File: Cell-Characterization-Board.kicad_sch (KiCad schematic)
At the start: 1 part, among them U1 ESP32-S3-WROOM-1

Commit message: 🤪
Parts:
- added D1, D2, D3, D4: SBR10E45P5-7, SBR10E45P57, symbol SBR10E45P5-7:SBR10E45P5-7
- added IC1, IC2, IC3, IC4: CPC1006N, SOP254P610X216-4N, symbol CPC1006N:CPC1006N
- added K1, K2, K3, K4: V23105A5001A201, V23105A5001A201, symbol V23105A5001A201:V23105A5001A201
- added RT1, RT2, RT3, RT4: NCP18XH103F03RB, THRMC1608X95N, symbol NCP18XH103F03RB:NCP18XH103F03RB
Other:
- added sheet ADC (ADC.kicad_sch)
- added sheet Cell1 (Cell.kicad_sch)
- added sheet Cell2 (Cell.kicad_sch)
- added sheet Cell3 (Cell.kicad_sch)
- added sheet Cell4 (Cell.kicad_sch)
- added sheet Power (Power.kicad_sch)
- moved on the sheet: U1

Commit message: Updated main schematic
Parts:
- removed D1, D2, D3, D4: SBR10E45P5-7, SBR10E45P57, symbol SBR10E45P5-7:SBR10E45P5-7
- removed IC1, IC2, IC3, IC4: CPC1006N, SOP254P610X216-4N, symbol CPC1006N:CPC1006N
- removed K1, K2, K3, K4: V23105A5001A201, V23105A5001A201, symbol V23105A5001A201:V23105A5001A201
- removed RT1, RT2, RT3, RT4: NCP18XH103F03RB, THRMC1608X95N, symbol NCP18XH103F03RB:NCP18XH103F03RB
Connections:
- net GND: now also U1.1 (GND), U1.40 (GND), U1.41 (GND)
- net GPIO17: now reaches U1.10 (IO17)
- net GPIO18: now reaches U1.11 (IO18)
- net PWM2: now reaches U1.12 (IO8)
- net ADC1_2: now reaches U1.15 (IO3)
- net PWM1: now reaches U1.17 (IO9)
- net PWM0: now reaches U1.18 (IO10)
- net ADC2_0: now reaches U1.19 (IO11)
- net +3V3: now reaches U1.2 (3V3)
- net ADC2_1: now reaches U1.20 (IO12)
- net ADC2_2: now reaches U1.21 (IO13)
- net ADC2_3: now reaches U1.22 (IO14)
- net GPIO0: now reaches U1.27 (IO0)
- net ADC1_1: now reaches U1.31 (IO38)
- net ADC1_0: now reaches U1.32 (IO39)
- net GPIO2: now reaches U1.38 (IO2)
- net GPIO1: now reaches U1.39 (IO1)
- net ADC1_3: now reaches U1.4 (IO4)
- net GPIO5: now reaches U1.5 (IO5)
- net GPIO6: now reaches U1.6 (IO6)
- net PWM3: now reaches U1.7 (IO7)
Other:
- note added: "INT"
- moved on the sheet: U1

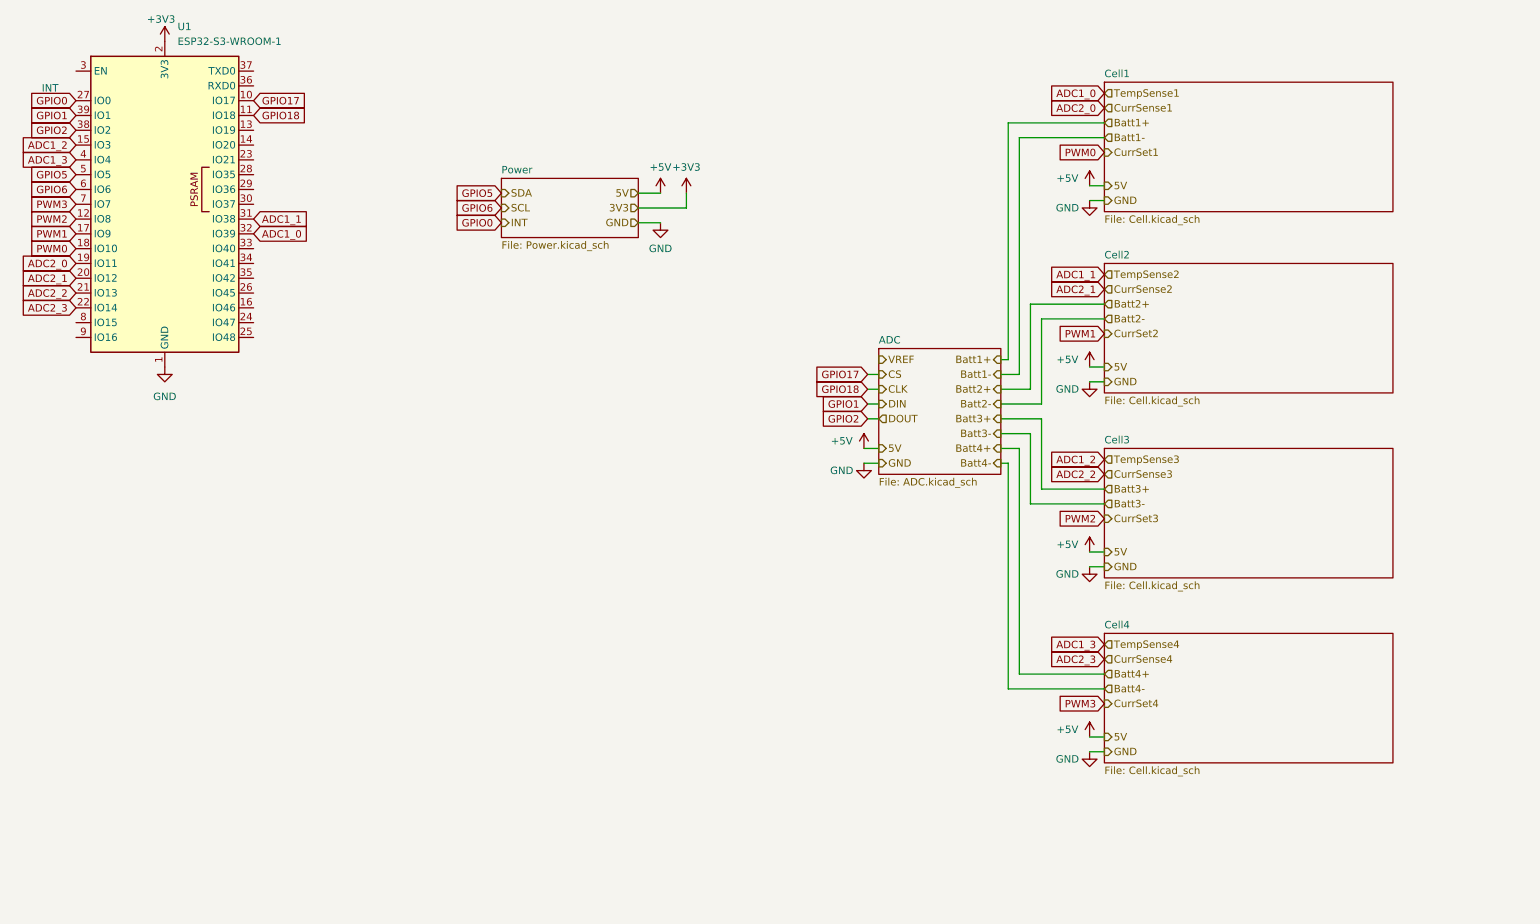
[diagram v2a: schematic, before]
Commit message: Added a few more components to the sch
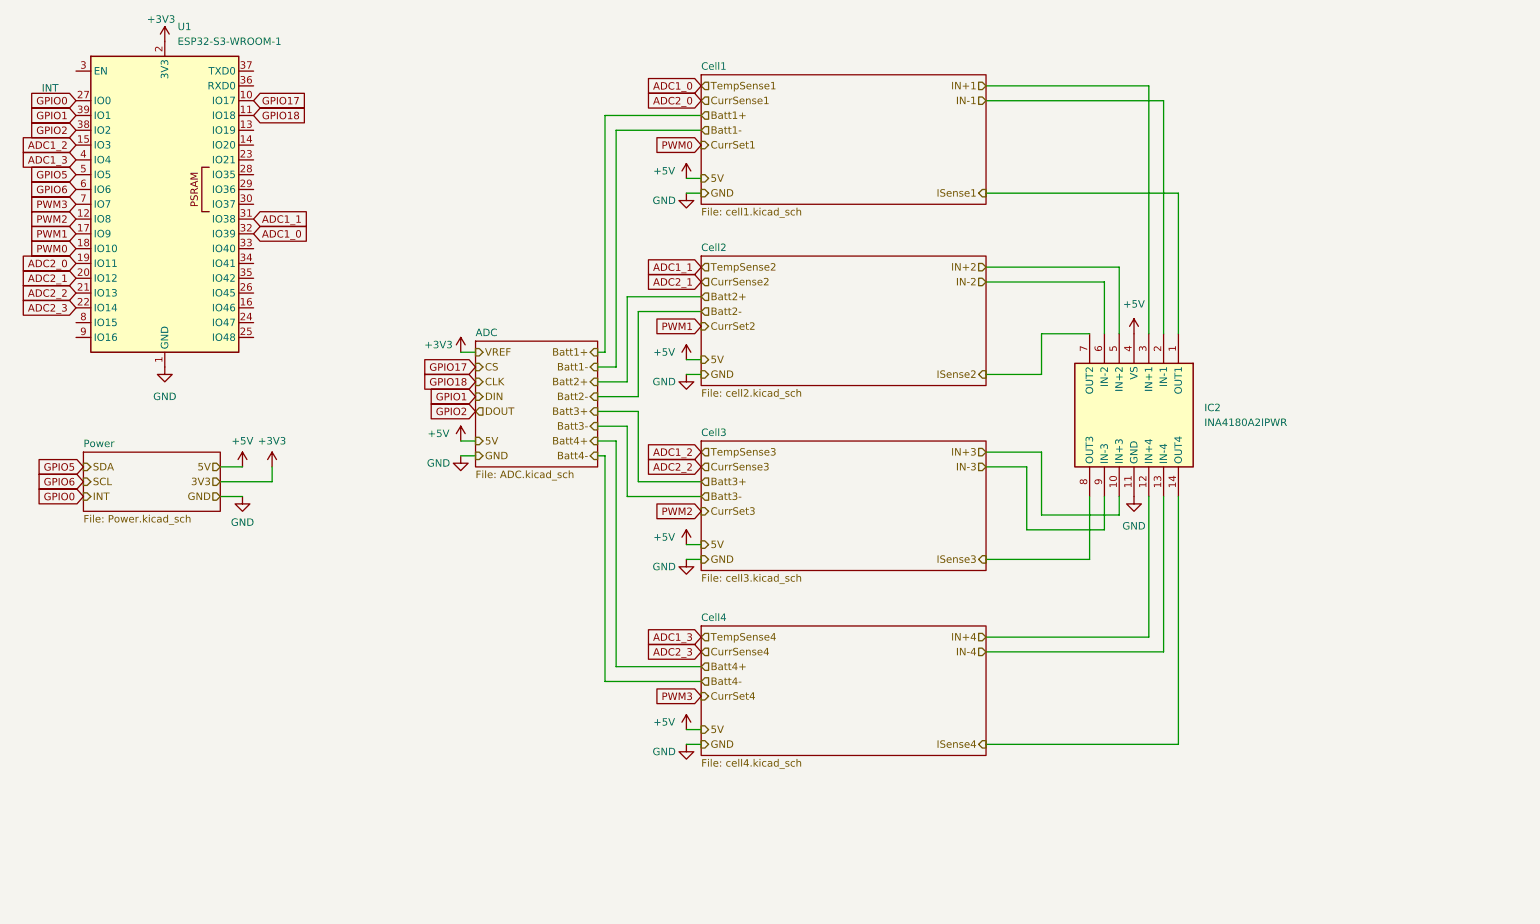
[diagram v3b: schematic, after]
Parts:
- added IC2: INA4180A2IPWR, SOP65P640X120-14N, symbol INA4180A2IPWR:INA4180A2IPWR
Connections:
- net +5V: now also IC2.4 (VS)
- net GND: now also IC2.11 (GND)
- new net IN+1: IC2.3 (IN+1)
- new net IN+2: IC2.5 (IN+2)
- new net IN+3: IC2.10 (IN+3)
- new net IN+4: IC2.12 (IN+4)
- new net IN-1: IC2.2 (IN-1)
- new net IN-2: IC2.6 (IN-2)
- new net IN-3: IC2.9 (IN-3)
- new net IN-4: IC2.13 (IN-4)
- new net ISense1: IC2.1 (OUT1)
- new net ISense2: IC2.7 (OUT2)
- new net ISense3: IC2.8 (OUT3)
- new net ISense4: IC2.14 (OUT4)
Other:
- sheet Cell1: file Cell.kicad_sch -> cell1.kicad_sch
- sheet Cell2: file Cell.kicad_sch -> cell2.kicad_sch
- sheet Cell3: file Cell.kicad_sch -> cell3.kicad_sch
- sheet Cell4: file Cell.kicad_sch -> cell4.kicad_sch

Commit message: updated power stuff
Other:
- note added: "ESP32"
- note added: "External ADC"
- note added: "Individual Cell Modules"
- note added: "USB-C PD Power Delivery"
- moved on the sheet: IC2, U1

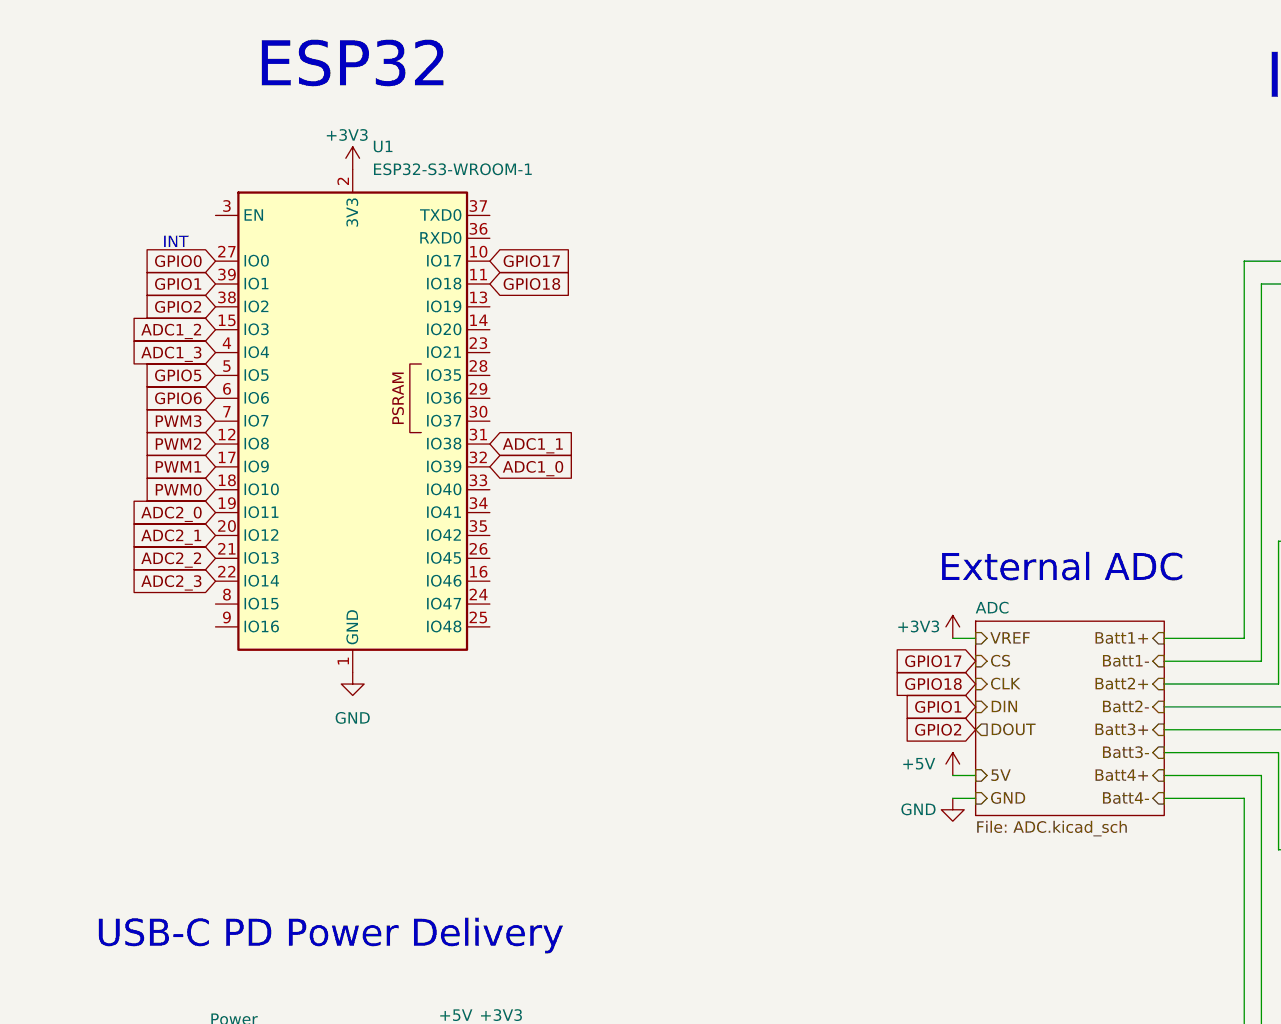
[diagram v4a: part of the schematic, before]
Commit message: began adding USB-UART bridge
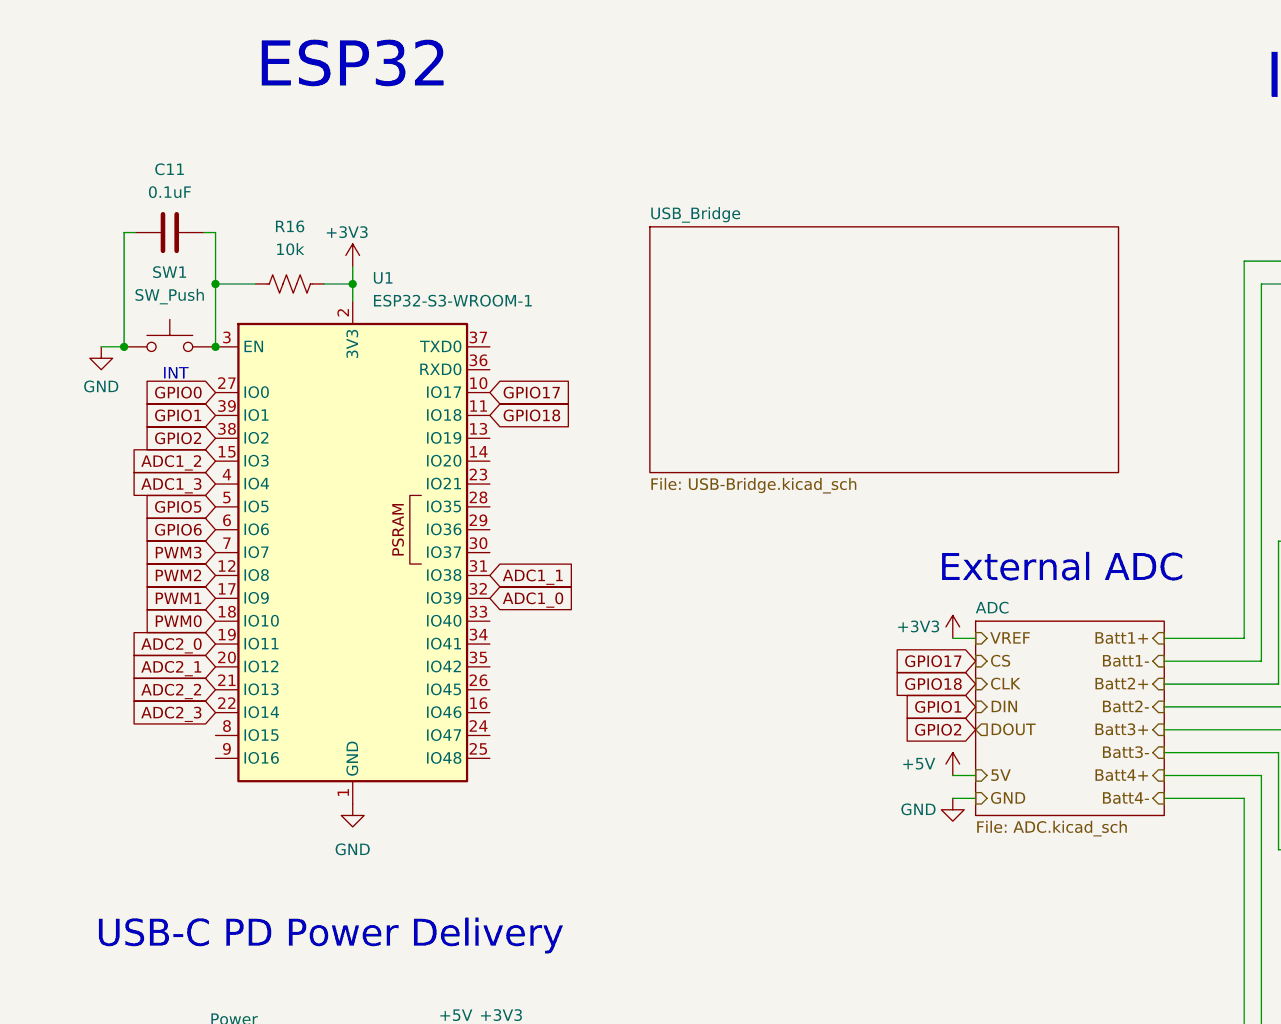
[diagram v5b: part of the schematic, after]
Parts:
- added C11: 0.1uF, symbol Device:C
- added R16: 10k, symbol Device:R_US
- added SW1: SW_Push, symbol Switch:SW_Push
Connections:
- net +3V3: now also R16.2
- net GND: now also C11.1, SW1.1
- net at U1.3 (EN): now also C11.2, R16.1, SW1.2
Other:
- added sheet USB_Bridge (USB-Bridge.kicad_sch)
- moved on the sheet: U1

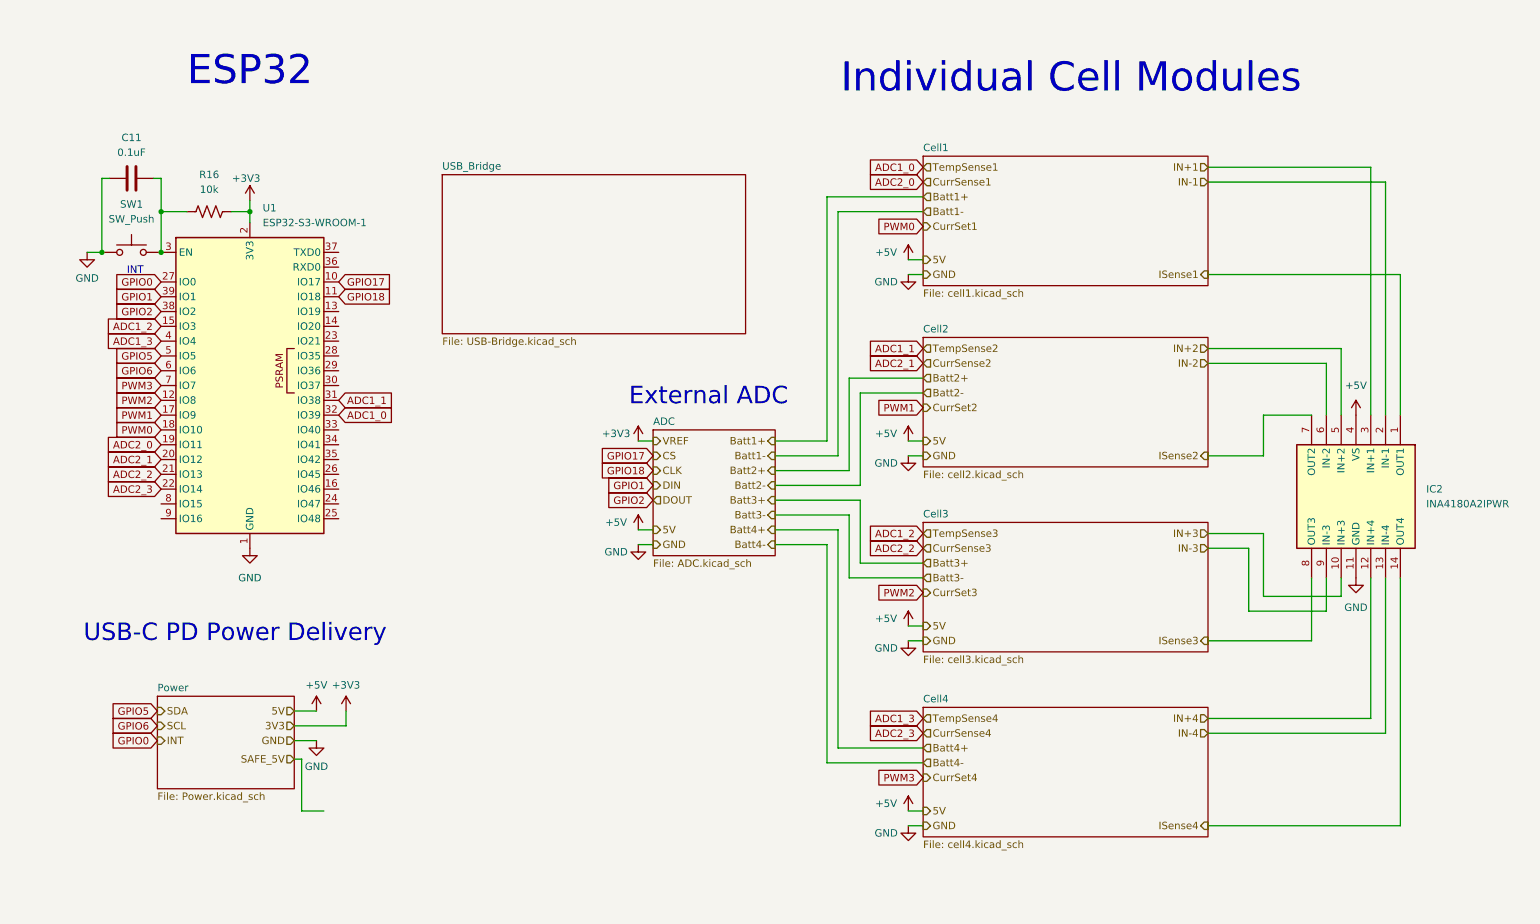
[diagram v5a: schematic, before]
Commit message: usb uart fixes and ldo
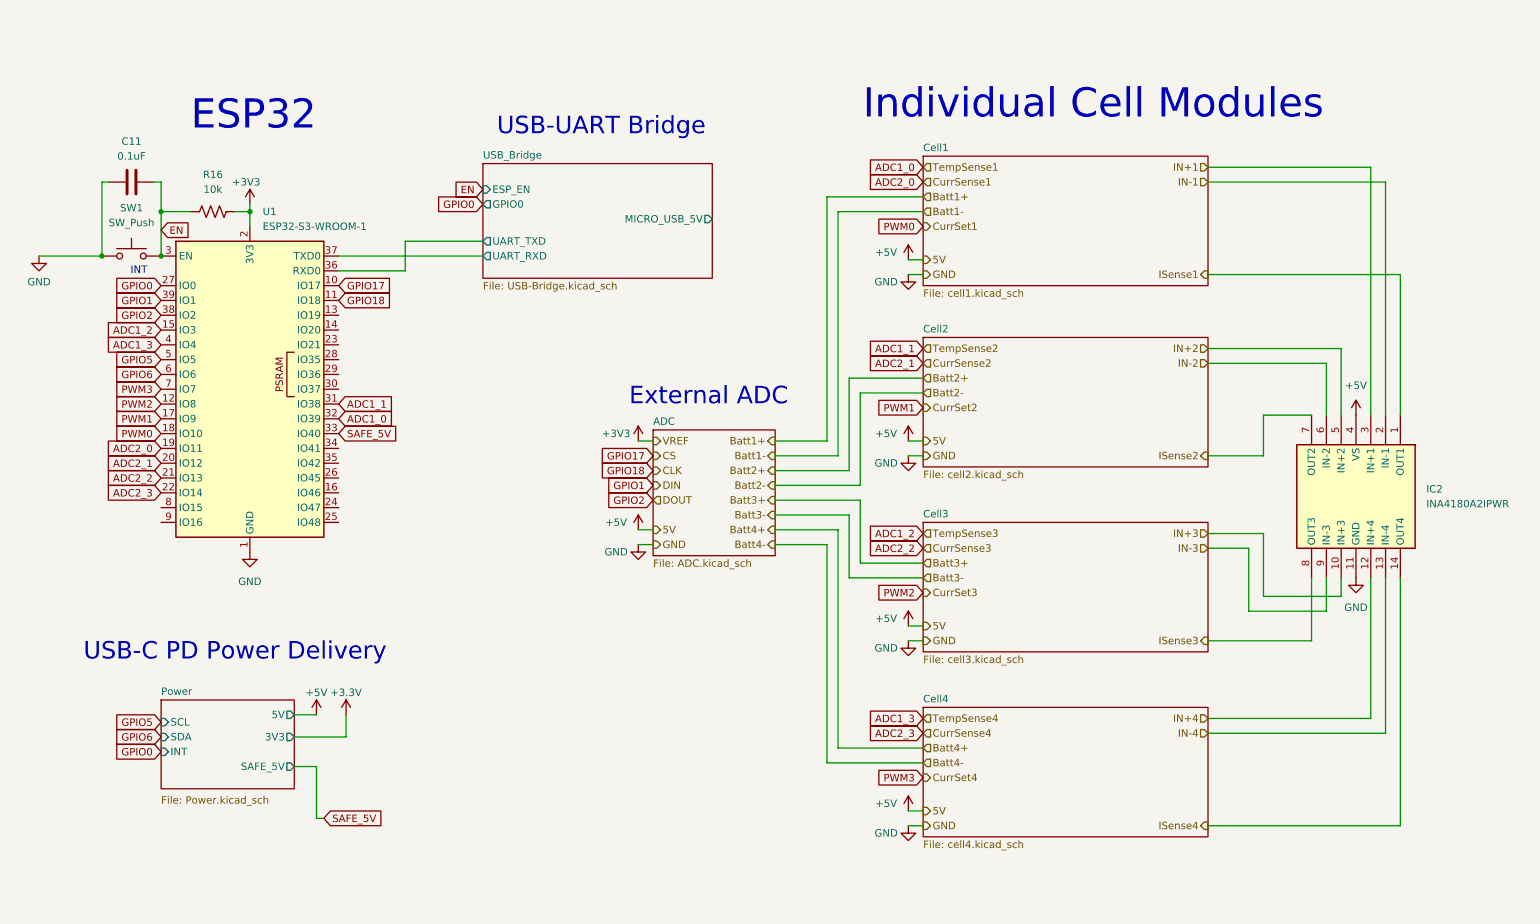
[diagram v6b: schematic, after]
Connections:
- net SAFE_5V: now also U1.33 (IO40)
- net EN: now reaches C11.2, R16.1, SW1.2, U1.3 (EN)
- net USB_Bridge/UART_TXD: now reaches U1.36 (RXD0)
- net USB_Bridge/UART_RXD: now reaches U1.37 (TXD0)
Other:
- sheet Power ports: added 3V3, 5V, INT, SAFE_5V, SCL, SDA; removed none
- sheet USB_Bridge ports: added ESP_EN, GPIO0, MICRO_USB_5V, UART_RXD, UART_TXD; removed none
- note added: "USB-UART Bridge"
- moved on the sheet: C11, R16, SW1, U1
